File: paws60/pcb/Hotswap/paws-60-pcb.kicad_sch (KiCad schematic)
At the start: 18 parts, among them J1 JST SH 4-pin, J2 AVR-ISP-6, SW1 Reset, U1 SRV05-4, U2 ATmega32U4-AU, Y1 16MHz

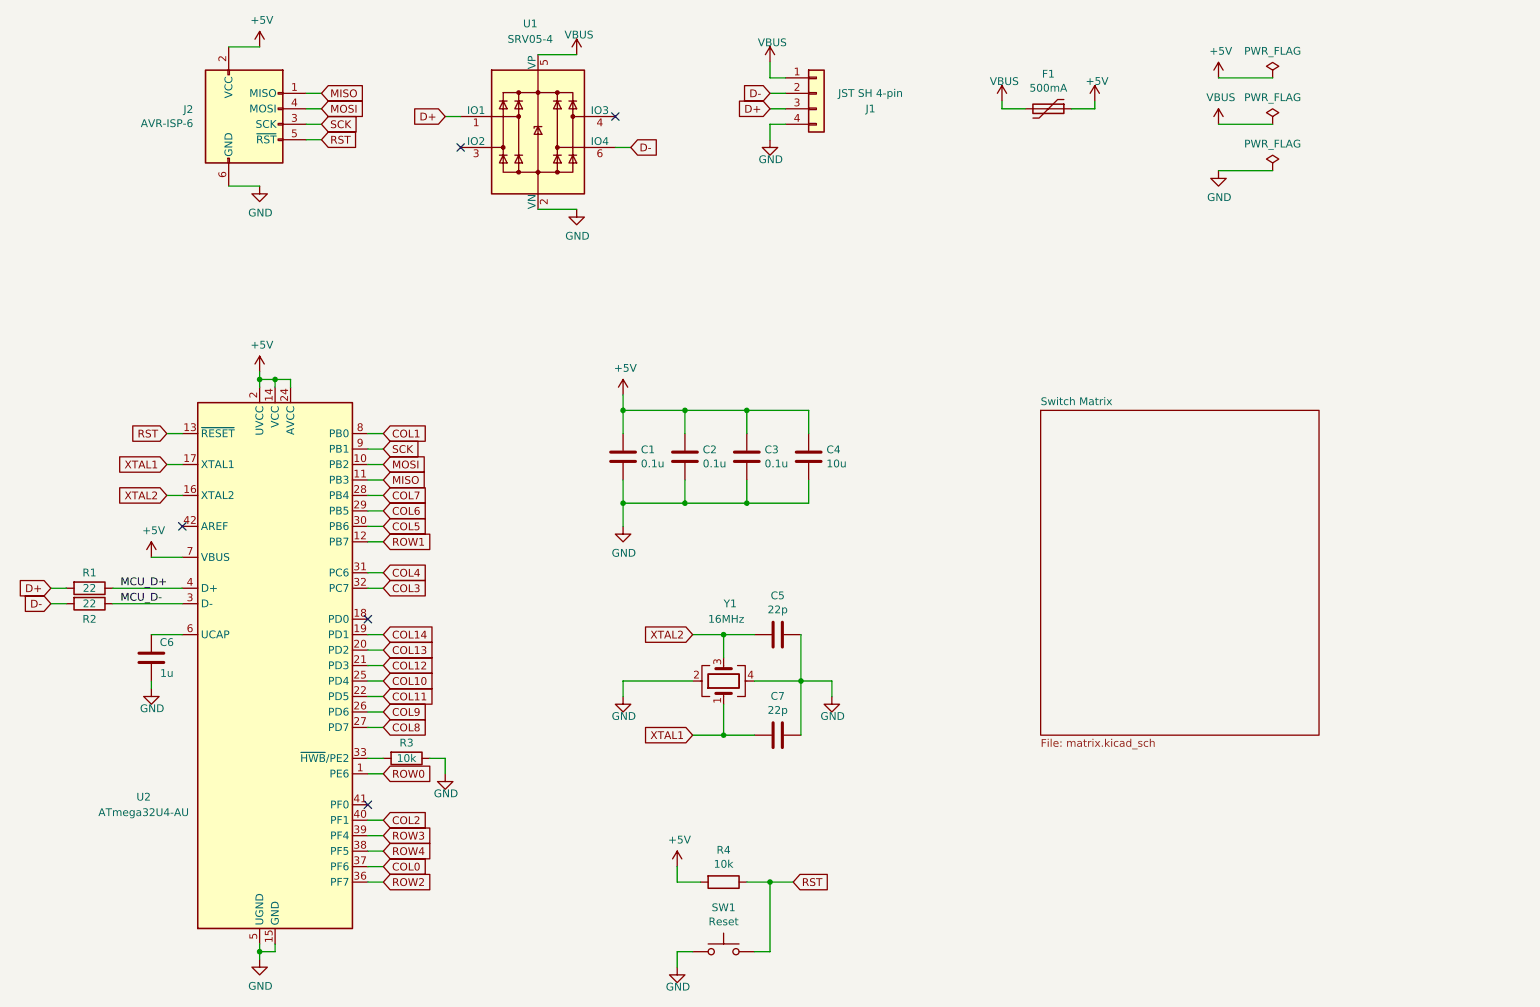
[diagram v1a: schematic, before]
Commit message: Added USB-C port, still not sure it correct or not
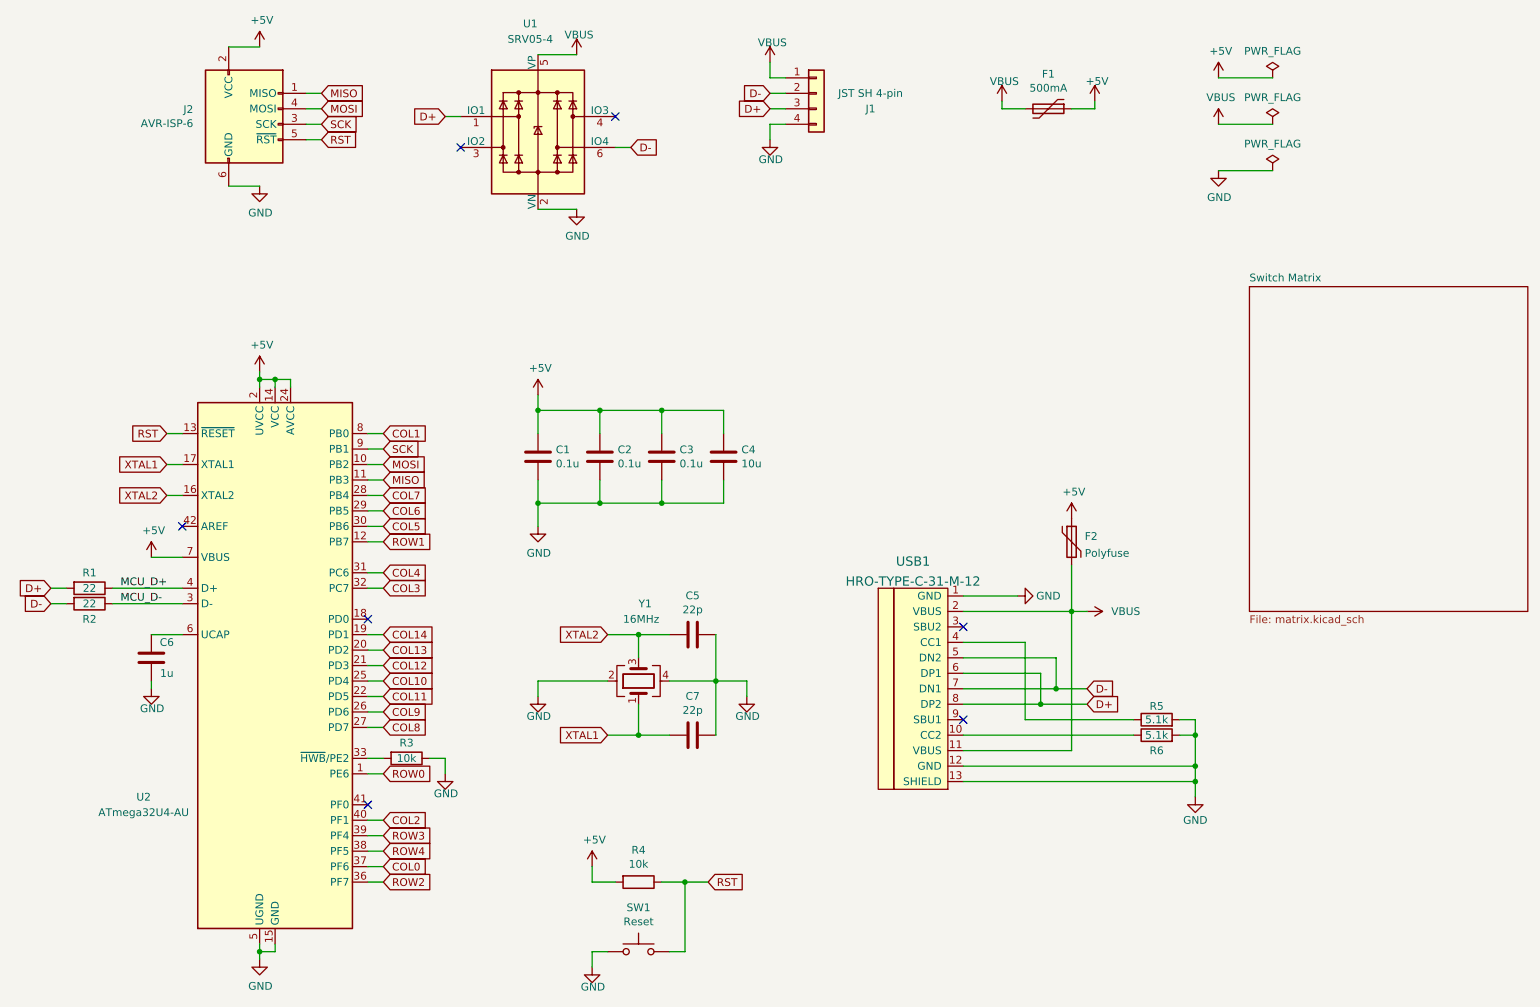
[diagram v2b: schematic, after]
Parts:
- added F2: Polyfuse, Resistor_SMD:R_0805_2012Metric, symbol Device:Polyfuse
- added R5, R6: 5.1k, Resistor_SMD:R_0805_2012Metric, symbol Device:R
- added USB1: HRO-TYPE-C-31-M-12, Type-C:HRO-TYPE-C-31-M-12, symbol Type-C:HRO-TYPE-C-31-M-12
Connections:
- net +5V: now also F2.1
- net D+: now also USB1.6 (DP1), USB1.8 (DP2)
- net D-: now also USB1.5 (DN2), USB1.7 (DN1)
- net GND: now also R5.2, R6.2, USB1.1 (GND), USB1.12 (GND), USB1.13 (SHIELD)
- net VBUS: now also F2.2, USB1.11 (VBUS), USB1.2 (VBUS)
- new net: R6.1, USB1.10 (CC2)
- new net: R5.1, USB1.4 (CC1)
- no-connect marks 5 -> 7
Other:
- moved on the sheet: C1, C2, C3, C4, C5, C7, R4, SW1, Y1

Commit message: Change new mount, blah blah...
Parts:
- added S1: Screw_Left, Type-C:10x5_7x2.5mm, symbol Connector:Screw_Terminal_01x01
- added S2: Screw_Right, Type-C:10x5_7x2.5mm, symbol Connector:Screw_Terminal_01x01
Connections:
- no-connect marks 7 -> 9
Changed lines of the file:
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@@
     (comment 2 "MIT License")
   )
+  (junction (at 116.84 88.9) (diameter 0) (color 0 0 0 0))
+  (junction (at 63.5 83.82) (diameter 0) (color 0 0 0 0))
+  (junction (at 123.19 125.73) (diameter 0) (color 0 0 0 0))
+  (junction (at 127 104.14) (diameter 0) (color 0 0 0 0))
+  (junction (at 123.19 142.24) (diameter 0) (color 0 0 0 0))
+  (junction (at 191.77 134.62) (diameter 0) (color 0 0 0 0))
+  (junction (at 60.96 83.82) (diameter 0) (color 0 0 0 0))
   (junction (at 106.68 104.14) (diameter 0) (color 0 0 0 0))
-  (junction (at 123.19 142.24) (diameter 0) (color 0 0 0 0))
+  (junction (at 214.63 142.24) (diameter 0) (color 0 0 0 0))
+  (junction (at 116.84 104.14) (diameter 0) (color 0 0 0 0))
   (junction (at 106.68 88.9) (diameter 0) (color 0 0 0 0))
-  (junction (at 116.84 88.9) (diameter 0) (color 0 0 0 0))
-  (junction (at 214.63 142.24) (diameter 0) (color 0 0 0 0))
   (junction (at 194.31 121.92) (diameter 0) (color 0 0 0 0))
-  (junction (at 60.96 177.8) (diameter 0) (color 0 0 0 0))
-  (junction (at 127 104.14) (diameter 0) (color 0 0 0 0))
   (junction (at 130.81 166.37) (diameter 0) (color 0 0 0 0))
-  (junction (at 191.77 134.62) (diameter 0) (color 0 0 0 0))
-  (junction (at 63.5 83.82) (diameter 0) (color 0 0 0 0))
+  (junction (at 214.63 147.32) (diameter 0) (color 0 0 0 0))
   (junction (at 214.63 149.86) (diameter 0) (color 0 0 0 0))
   (junction (at 127 88.9) (diameter 0) (color 0 0 0 0))
-  (junction (at 60.96 83.82) (diameter 0) (color 0 0 0 0))
   (junction (at 135.89 133.35) (diameter 0) (color 0 0 0 0))
-  (junction (at 214.63 147.32) (diameter 0) (color 0 0 0 0))
-  (junction (at 116.84 104.14) (diameter 0) (color 0 0 0 0))
   (junction (at 189.23 137.16) (diameter 0) (color 0 0 0 0))
-  (junction (at 123.19 125.73) (diameter 0) (color 0 0 0 0))
+  (junction (at 60.96 177.8) (diameter 0) (color 0 0 0 0))
   (no_connect (at 78.74 153.67))
   (no_connect (at 48.26 107.95))
   (no_connect (at 176.53 139.7))
   (no_connect (at 119.38 40.64))
+  (no_connect (at 166.37 63.5))
+  (no_connect (at 166.37 69.85))
   (no_connect (at 78.74 123.19))
   (no_connect (at 176.53 124.46))
@@
     (stroke (width 0) (type default) (color 0 0 0 0))
   )
+  (wire (pts (xy 176.53 127) (xy 186.69 127))
+    (stroke (width 0) (type default) (color 0 0 0 0))
+  )
+  (wire (pts (xy 186.69 127) (xy 186.69 139.7))
+    (stroke (width 0) (type default) (color 0 0 0 0))
+  )
   (wire (pts (xy 186.69 139.7) (xy 204.47 139.7))
     (stroke (width 0) (type default) (color 0 0 0 0))
   )
-  (wire (pts (xy 176.53 127) (xy 186.69 127))
-    (stroke (width 0) (type default) (color 0 0 0 0))
-  )
-  (wire (pts (xy 186.69 127) (xy 186.69 139.7))
-    (stroke (width 0) (type default) (color 0 0 0 0))
-  )
   (wire (pts (xy 63.5 177.8) (xy 63.5 176.53))
     (stroke (width 0) (type default) (color 0 0 0 0))
@@
     (stroke (width 0) (type default) (color 0 0 0 0))
   )
+  (wire (pts (xy 212.09 139.7) (xy 214.63 139.7))
+    (stroke (width 0) (type default) (color 0 0 0 0))
+  )
+  (wire (pts (xy 214.63 139.7) (xy 214.63 142.24))
+    (stroke (width 0) (type default) (color 0 0 0 0))
+  )
   (wire (pts (xy 214.63 149.86) (xy 214.63 152.4))
     (stroke (width 0) (type default) (color 0 0 0 0))
@@
     (stroke (width 0) (type default) (color 0 0 0 0))
   )
-  (wire (pts (xy 212.09 139.7) (xy 214.63 139.7))
-    (stroke (width 0) (type default) (color 0 0 0 0))
-  )
-  (wire (pts (xy 214.63 139.7) (xy 214.63 142.24))
-    (stroke (width 0) (type default) (color 0 0 0 0))
-  )
   (wire (pts (xy 176.53 147.32) (xy 214.63 147.32))
     (stroke (width 0) (type default) (color 0 0 0 0))
@@
     (stroke (width 0) (type default) (color 0 0 0 0))
   )
+  (wire (pts (xy 176.53 129.54) (xy 191.77 129.54))
+    (stroke (width 0) (type default) (color 0 0 0 0))
+  )
   (wire (pts (xy 191.77 129.54) (xy 191.77 134.62))
     (stroke (width 0) (type default) (color 0 0 0 0))
   )
-  (wire (pts (xy 176.53 129.54) (xy 191.77 129.54))
-    (stroke (width 0) (type default) (color 0 0 0 0))
-  )
   (wire (pts (xy 227.33 34.29) (xy 218.44 34.29))
     (stroke (width 0) (type default) (color 0 0 0 0))
@@
     (stroke (width 0) (type default) (color 0 0 0 0))
   )
+  (wire (pts (xy 176.53 132.08) (xy 189.23 132.08))
+    (stroke (width 0) (type default) (color 0 0 0 0))
+  )
   (wire (pts (xy 189.23 132.08) (xy 189.23 137.16))
     (stroke (width 0) (type default) (color 0 0 0 0))
   )
-  (wire (pts (xy 176.53 132.08) (xy 189.23 132.08))
-    (stroke (width 0) (type default) (color 0 0 0 0))
-  )
   (wire (pts (xy 137.16 88.9) (xy 127 88.9))
     (stroke (width 0) (type default) (color 0 0 0 0))
@@
     (stroke (width 0) (type default) (color 0 0 0 0))
   )
+  (wire (pts (xy 176.53 121.92) (xy 194.31 121.92))
+    (stroke (width 0) (type default) (color 0 0 0 0))
+  )
   (wire (pts (xy 194.31 121.92) (xy 196.85 121.92))
-    (stroke (width 0) (type default) (color 0 0 0 0))
-  )
-  (wire (pts (xy 176.53 121.92) (xy 194.31 121.92))
     (stroke (width 0) (type default) (color 0 0 0 0))
   )
@@
     (pin "1")
   )
+  (symbol (lib_id "Connector:Screw_Terminal_01x01") (at 171.45 63.5 0) (unit 1)
+    (in_bom yes) (on_board yes) (fields_autoplaced)
+    (property "Reference" "S1" (id 0) (at 173.482 62.5915 0)
+      (effects (font (size 1.27 1.27)) (justify left))
+    )
+    (property "Value" "Screw_Left" (id 1) (at 173.482 65.3666 0)
+      (effects (font (size 1.27 1.27)) (justify left))
+    )
+    (property "Footprint" "Type-C:10x5_7x2.5mm" (id 2) (at 171.45 63.5 0)
+      (effects (font (size 1.27 1.27)) hide)
+    )
+    (property "Datasheet" "~" (id 3) (at 171.45 63.5 0)
+      (effects (font (size 1.27 1.27)) hide)
+    )
+    (pin "1")
+  )
   (symbol (lib_name "R_1") (lib_id "Device:R") (at 208.28 139.7 90) (unit 1)
     (in_bom yes) (on_board yes)
@@
     (pin "1")
     (pin "2")
+  )
+  (symbol (lib_id "Connector:Screw_Terminal_01x01") (at 171.45 69.85 0) (unit 1)
+    (in_bom yes) (on_board yes) (fields_autoplaced)
+    (property "Reference" "S2" (id 0) (at 173.482 68.9415 0)
+      (effects (font (size 1.27 1.27)) (justify left))
+    )
+    (property "Value" "Screw_Right" (id 1) (at 173.482 71.7166 0)
+      (effects (font (size 1.27 1.27)) (justify left))
+    )
+    (property "Footprint" "Type-C:10x5_7x2.5mm" (id 2) (at 171.45 69.85 0)
+      (effects (font (size 1.27 1.27)) hide)
+    )
+    (property "Datasheet" "~" (id 3) (at 171.45 69.85 0)
+      (effects (font (size 1.27 1.27)) hide)
+    )
+    (pin "1")
   )
   (symbol (lib_name "Polyfuse_1") (lib_id "Device:Polyfuse") (at 194.31 110.49 0) (unit 1)
@@
       (reference "R6") (unit 1) (value "5.1k") (footprint "Resistor_SMD:R_0805_2012Metric")
     )
+    (path "/9f2fd9e7-880f-4692-af4b-0d2ac9a8dc90"
+      (reference "S1") (unit 1) (value "Screw_Left") (footprint "Type-C:10x5_7x2.5mm")
+    )
+    (path "/b31702c5-548d-4cd7-a92d-2f3586af42f0"
+      (reference "S2") (unit 1) (value "Screw_Right") (footprint "Type-C:10x5_7x2.5mm")
+    )
     (path "/00000000-0000-0000-0000-00005f27b00d"

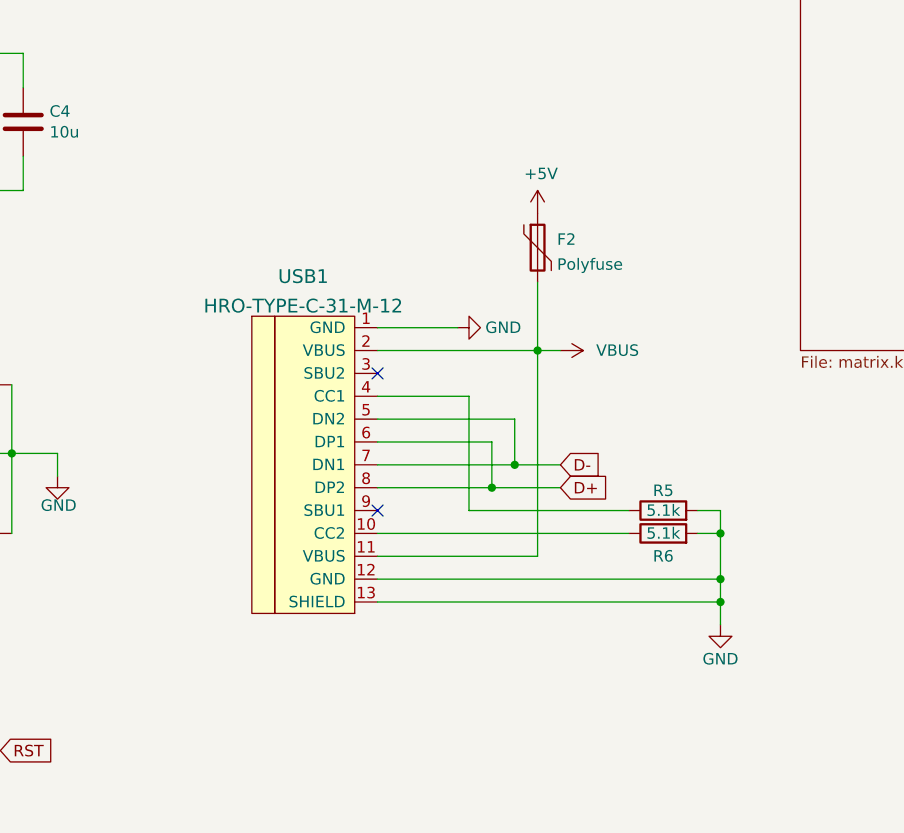
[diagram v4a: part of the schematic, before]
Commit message: Add logo, and remove usb-c.
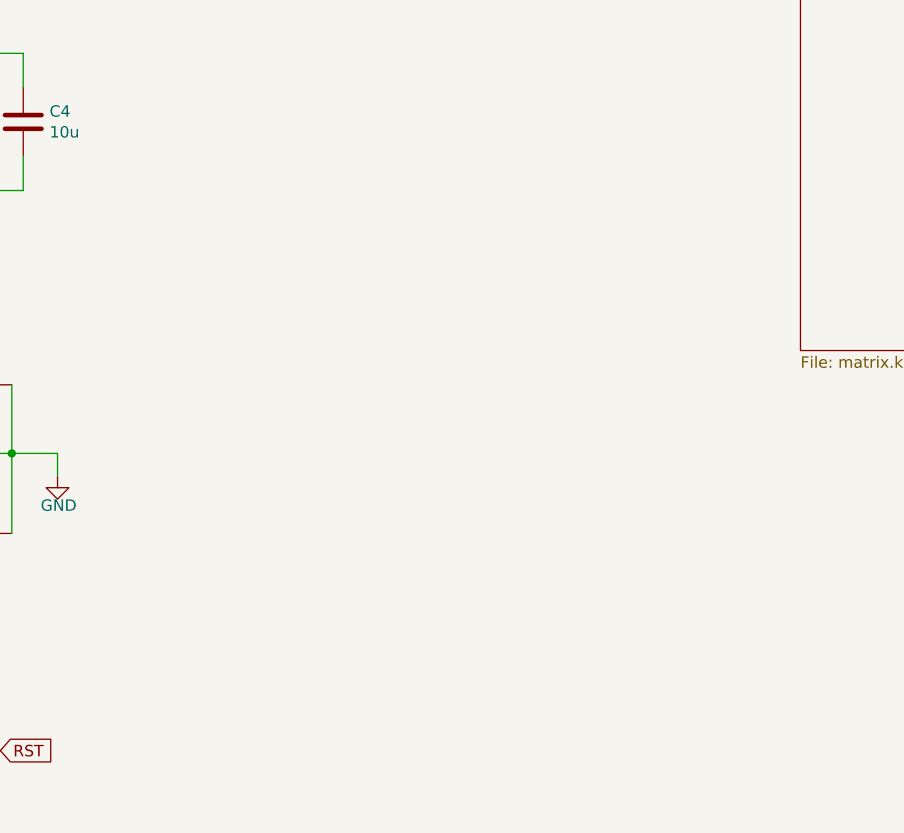
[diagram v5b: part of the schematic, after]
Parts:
- removed F2: Polyfuse, Resistor_SMD:R_0805_2012Metric, symbol Device:Polyfuse
- removed R5, R6: 5.1k, Resistor_SMD:R_0805_2012Metric, symbol Device:R
- removed USB1: HRO-TYPE-C-31-M-12, Type-C:HRO-TYPE-C-31-M-12, symbol Type-C:HRO-TYPE-C-31-M-12
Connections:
- no-connect marks 9 -> 7
